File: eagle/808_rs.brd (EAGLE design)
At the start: 100 x 80 mm, 75 parts, among them IC1 TL072P, IC2 TL072P, Q1 2SK30, Q59 2N3904, Q60 2N3906, Q61 2N3904, Q62 2N3904, Q63 2N3904, SW8 808_LT_MSS42_SW_4PDT

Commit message: 95pct auto
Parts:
- C113: device TR808clone:C050-024X044 -> TR808clone:C075-032X103
- C114: device TR808clone:C035-025X75 -> TR808clone:C050-030X075
- C121: device TR808clone:C035-025X75 -> TR808clone:C050-025X075
- C4: device TR808clone:C025-025X050 -> TR808clone:C050-024X044
- D61, D63, D64: value 1N4148DO35-7 -> 1N4148DO35-10; device TR808clone:DO35-7 -> TR808clone:DO35-10
- R303, R309, R330: device TR808clone:0207/5V -> TR808clone:0207/2V
- R316: device TR808clone:0207/7 -> TR808clone:0207/5V
- R321: device TR808clone:0207/5V -> TR808clone:0207/7
- R326: device TR808clone:0207/7 -> TR808clone:0309/10
- moved C2 7.62 mm to (67.3, 15.2), turned to 90 degrees
- moved Q61 6.84 mm to (22.9, 15.2)
- moved C112 5.68 mm to (30.5, 19.1), turned to 90 degrees
- moved R238 5.68 mm to (76.2, 20.3), turned to 180 degrees
- moved R304 5.39 mm to (24.1, 21.6)
- moved R305 5.24 mm to (43.2, 20.3)
- moved C153 4.02 mm to (61.0, 15.2)
- moved IC2 4.02 mm to (61.0, 21.6)
- moved R330 4.02 mm to (61.0, 12.7)
- moved OUT_NORM 4.02 mm to (77.5, 14.0), turned to 90 degrees
- moved R331 4.02 mm to (50.8, 20.3)
- moved C113 3.81 mm to (47.0, 20.3)
- moved C121 3.81 mm to (34.3, 36.8)
- moved C4 2.84 mm to (53.3, 26.7), turned to 180 degrees
- moved R316 2.84 mm to (63.5, 53.3)
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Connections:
- net N$172: now also C121.1; no longer C121.P$1
- net N$173: now also C114.1; no longer C114.P$1
- net N$328: now also C121.2; no longer C121.P$2
- net N$357: now also C114.2; no longer C114.P$2
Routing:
- net -12V: track 28.9 -> 268.6 mm
- net GND: track 346.2 -> 255.4 mm
- net N$357: track 44.0 -> 110.3 mm
- net N$338: track 120.2 -> 64.0 mm
- net N$351: track 87.8 -> 65.8 mm
- net N$348: track 50.0 -> 34.2 mm
- net +12V: track 101.4 -> 89.6 mm
- net N$8: track 108.3 -> 117.2 mm
- net N$328: track 13.4 -> 8.74 mm
- net N$173: track 12.7 -> 8.15 mm
- net N$353: track 14.0 -> 10.4 mm
- net N$161: track 31.1 -> 34.0 mm
- net N$344: track 30.7 -> 27.8 mm
- net N$354: track 12.7 -> 10.2 mm
- net N$352: track 8.75 -> 6.35 mm
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
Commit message: 94pct auto
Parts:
- C118: device TR808clone:C035-025X75 -> TR808clone:C050-024X044
- C122: device TR808clone:C035-025X75 -> TR808clone:C050-030X075
- R318: device TR808clone:0207/2V -> TR808clone:0207/5V
- R320, R322: device TR808clone:0207/5V -> TR808clone:0207/7
- moved R316 6.48 mm to (57.1, 54.6), turned to 180 degrees
- moved R320 5.39 mm to (72.4, 49.5), turned to 270 degrees
- moved R299 5.08 mm to (16.5, 55.9), turned to 180 degrees
- moved R318 4.58 mm to (64.8, 54.6)
- moved C120 3.81 mm to (38.1, 25.4)
- moved ACCENT 3.81 mm to (17.8, 59.7)
- moved R301 2.84 mm to (48.3, 61.0)
- moved C125 2.84 mm to (81.3, 40.6)
- moved R317 2.84 mm to (69.8, 58.4)
- moved R238 2.84 mm to (78.7, 19.1)
- moved R297 2.54 mm to (7.62, 54.6), turned to 90 degrees
- moved C115 2.54 mm to (58.4, 58.4)
- moved C116 2.54 mm to (55.9, 58.4)
- moved Q62 2.54 mm to (40.6, 31.8)
- moved R310 2.54 mm to (43.2, 38.1)
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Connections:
- net N$165: now also C118.2; no longer C118.P$2
- net N$328: now also C122.1; no longer C122.P$1
- net N$329: now also C122.2; no longer C122.P$2
- net N$340: now also C118.1; no longer C118.P$1
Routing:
- net -12V: track 268.6 -> 0.00 mm
- net GND: track 255.4 -> 0.00 mm
- net N$8: track 117.2 -> 0.00 mm
- net N$357: track 110.3 -> 0.00 mm
- net +12V: track 89.6 -> 0.00 mm
- net N$6: track 66.3 -> 0.00 mm
- net N$351: track 65.8 -> 0.00 mm
- net N$338: track 64.0 -> 0.00 mm
- net N$355: track 44.8 -> 0.00 mm
- net TRIG: track 42.1 -> 0.00 mm
- net RS: track 35.3 -> 0.00 mm
- net N$348: track 34.2 -> 0.00 mm
- net N$161: track 34.0 -> 0.00 mm
- net N$165: track 28.6 -> 0.00 mm
- net N$344: track 27.8 -> 0.00 mm
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
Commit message: routed
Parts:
- C1: device TR808clone:C025-025X050 -> TR808clone:C050-024X044
- C112, C118: device TR808clone:C050-024X044 -> TR808clone:C050-025X075
- C113: device TR808clone:C075-032X103 -> TR808clone:C050-025X075
- C117, C119: device TR808clone:C035-025X75 -> TR808clone:C050-024X044
- C120: device TR808clone:E2,5-5 -> TR808clone:E2,5-6
- C125: device TR808clone:C035-025X75 -> TR808clone:C050-025X075
- R312, R314, R318: device TR808clone:0207/5V -> TR808clone:0207/7
- R331: device TR808clone:0207/7 -> TR808clone:0207/5V
- moved SW8 107.3 mm to (0.00, 14.0), turned to 270 degrees
- moved OUTPUT 103.5 mm to (0.00, 45.7), turned to 90 degrees
- moved VR16 92.7 mm to (3.81, 34.3), turned to 270 degrees
- moved R303 88.8 mm to (92.7, 19.1), turned to 270 degrees
- moved R297 88.4 mm to (92.7, 30.5), turned to 180 degrees
- moved U$1 86.1 mm to (90.2, 49.5), turned to 270 degrees
- moved ACCENT 83.9 mm to (82.5, 6.35), turned to 180 degrees
- moved R298 83.0 mm to (86.4, 12.7), turned to 180 degrees
- moved R299 81.4 mm to (83.8, 10.2), turned to 0 degrees
- moved TRIGGER 80.1 mm to (87.6, 31.5), turned to 180 degrees
- moved Q59 80.0 mm to (87.6, 19.1), turned to 270 degrees
- moved R306 77.3 mm to (89.2, 26.7), turned to 0 degrees
- moved Q60 71.7 mm to (81.3, 15.2), turned to 180 degrees
- moved C111 71.0 mm to (74.9, 6.35), turned to 270 degrees
- moved C114 70.8 mm to (83.6, 21.6), turned to 270 degrees
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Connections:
- net N$2: now also C125.1; no longer C125.P$1
- net N$338: now also C117.2, C119.1; no longer C117.P$2, C119.P$1
- net N$339: now also C119.2; no longer C119.P$2
- net N$340: now also C117.1; no longer C117.P$1
- net N$347: now also C125.2; no longer C125.P$2
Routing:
- net GND: track 0.00 -> 336.7 mm, vias 0 -> 2
- net +12V: track 0.00 -> 168.5 mm, vias 0 -> 6
- net -12V: track 0.00 -> 121.3 mm
- net N$8: track 0.00 -> 117.8 mm, vias 0 -> 2
- net N$351: track 0.00 -> 79.6 mm
- net N$6: track 0.00 -> 67.2 mm
- net N$355: track 0.00 -> 61.3 mm, vias 0 -> 2
- net N$338: track 0.00 -> 54.7 mm
- net N$357: track 0.00 -> 49.2 mm
- net TRIG: track 0.00 -> 46.0 mm
- net N$348: track 0.00 -> 37.5 mm
- net N$344: track 0.00 -> 31.4 mm
- net N$165: track 0.00 -> 27.3 mm
- net N$161: track 0.00 -> 21.1 mm
- net N$318: track 0.00 -> 18.1 mm
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
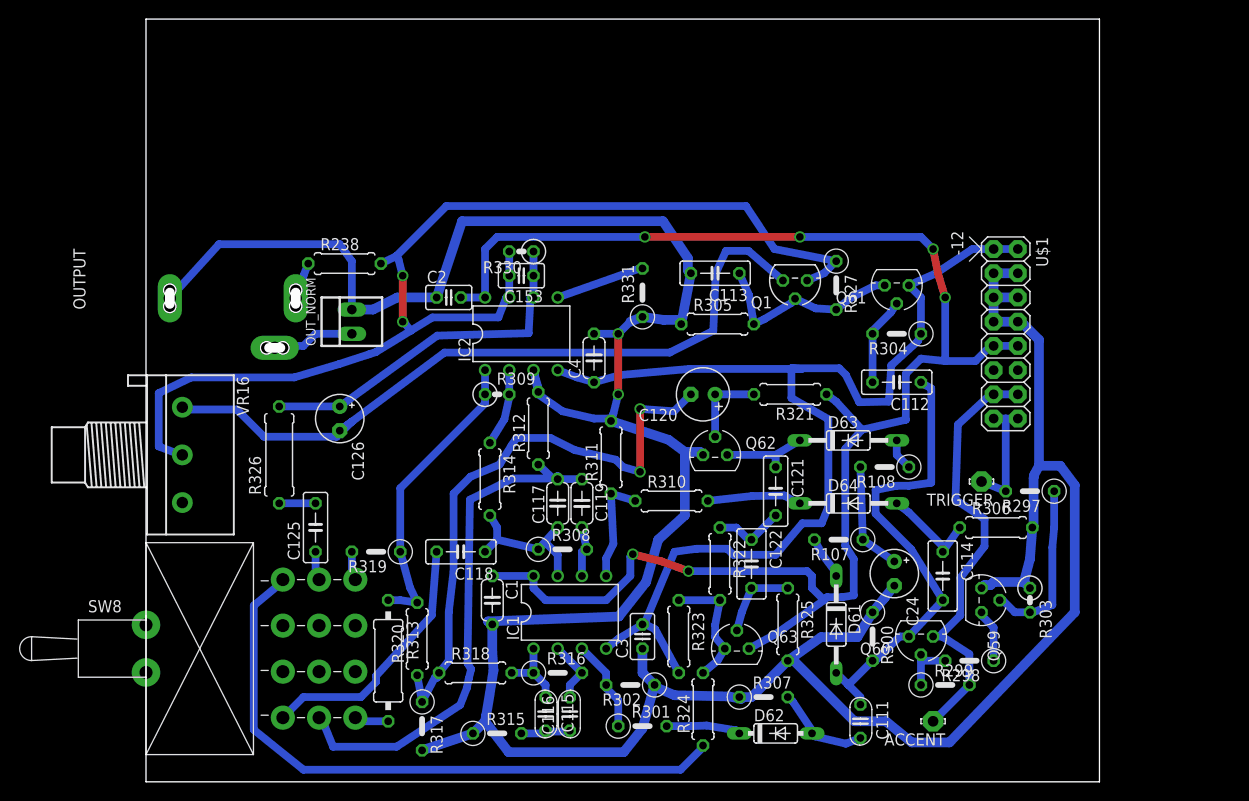
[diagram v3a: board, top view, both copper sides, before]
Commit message: almost rerouted
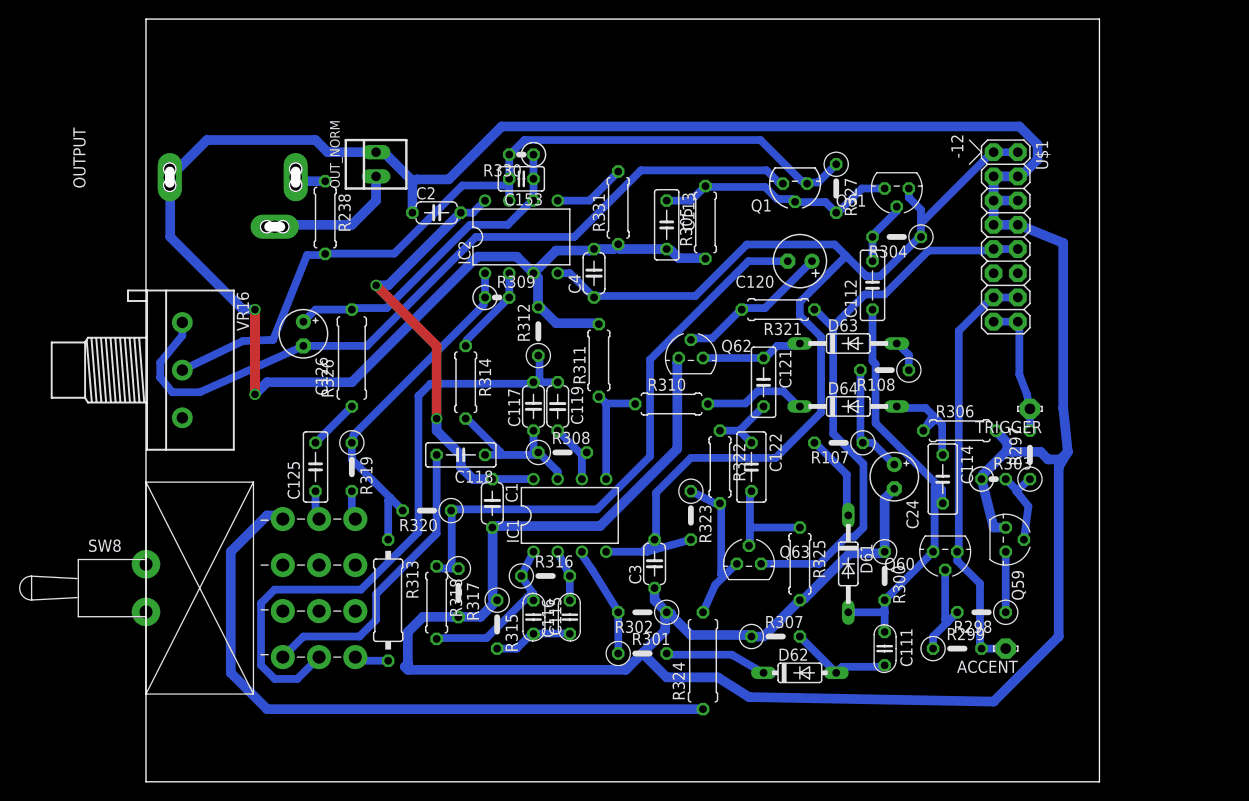
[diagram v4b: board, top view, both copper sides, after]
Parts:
- C2, C3: device TR808clone:C025-025X050 -> TR808clone:C050-024X044
- R312, R320, R323: device TR808clone:0207/7 -> TR808clone:0207/5V
- R324: device TR808clone:0207/7 -> TR808clone:0309/10
- R331: device TR808clone:0207/5V -> TR808clone:0207/7
- moved C120 17.3 mm to (68.6, 54.6)
- moved OUT_NORM 16.7 mm to (24.1, 64.8)
- moved R317 14.5 mm to (32.8, 19.8)
- moved R320 13.5 mm to (29.5, 28.4), turned to 180 degrees
- moved R303 13.3 mm to (88.9, 31.8), turned to 0 degrees
- moved R323 12.8 mm to (57.1, 27.9)
- moved OUTPUT 12.7 mm to (0.00, 58.4)
- moved R326 12.7 mm to (21.6, 44.5)
- moved C121 11.5 mm to (64.8, 41.9)
- moved R315 11.4 mm to (36.8, 16.5), turned to 270 degrees
- moved R306 10.9 mm to (85.3, 36.8)
- moved ACCENT 10.8 mm to (90.2, 14.0)
- moved R305 10.7 mm to (58.7, 58.7), turned to 90 degrees
- moved Q62 10.5 mm to (57.1, 44.5)
- moved C112 10.5 mm to (76.2, 52.1), turned to 90 degrees
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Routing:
- net GND: track 336.7 -> 450.6 mm
- net +12V: track 168.5 -> 106.2 mm, vias 6 -> 2
- net N$8: track 117.8 -> 86.6 mm, vias 2 -> 0
- net N$338: track 54.7 -> 66.1 mm
- net N$354: track 7.92 -> 18.0 mm
- net N$318: track 18.1 -> 9.20 mm
- net N$174: track 8.51 -> 16.1 mm
- net N$344: track 31.4 -> 37.3 mm
- net N$5: track 8.70 -> 14.3 mm
- net N$317: track 5.71 -> 10.4 mm
- net N$324: track 4.50 -> 9.10 mm
- net N$161: track 21.1 -> 25.6 mm
- net N$357: track 49.2 -> 44.9 mm
- net N$330: track 13.3 -> 17.5 mm
- net N$165: track 27.3 -> 31.3 mm
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
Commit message: rerouted
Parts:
- R320: device TR808clone:0207/5V -> TR808clone:0207/7
- moved C120 17.0 mm to (53.3, 47.0), turned to 270 degrees
- moved R107 4.31 mm to (75.7, 32.5)
- moved R314 4.10 mm to (37.6, 41.4)
- moved C24 3.84 mm to (79.0, 28.2)
- moved R323 2.54 mm to (57.1, 25.4)
- moved Q62 1.78 mm to (58.9, 44.5)
- moved C122 1.61 mm to (65.0, 33.5)
- moved R321 1.30 mm to (67.6, 49.8)
- moved R310 1.27 mm to (53.8, 39.6)
- moved R322 1.27 mm to (61.5, 33.0)
- moved R324 1.27 mm to (58.4, 14.0)
- moved R312 1.08 mm to (41.9, 46.5)
- moved R301 1.02 mm to (52.1, 14.5)
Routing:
- net +12V: track 106.2 -> 173.0 mm, vias 2 -> 4
- net N$355: track 60.6 -> 43.5 mm
- net -12V: track 119.0 -> 111.9 mm
- net GND: track 450.6 -> 444.4 mm
- net N$173: track 12.0 -> 7.14 mm
- net N$324: track 9.10 -> 4.79 mm
- net N$357: track 44.9 -> 48.1 mm
- net N$167: track 12.0 -> 15.0 mm
- net N$174: track 16.1 -> 13.4 mm
- net N$6: track 71.0 -> 68.5 mm
- net N$338: track 66.1 -> 63.9 mm
- net N$340: track 17.5 -> 15.4 mm
- net N$172: track 10.8 -> 9.03 mm
- net N$336: track 10.8 -> 12.3 mm
- net N$8: track 86.6 -> 88.0 mm
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
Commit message: tweaks
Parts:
- R305, R318: device TR808clone:0207/7 -> TR808clone:0207/5V
- R313: device TR808clone:0309/12 -> TR808clone:0207/7
- R316: device TR808clone:0207/5V -> TR808clone:0207/2V
- R324: device TR808clone:0309/10 -> TR808clone:0207/7
- moved R318 6.67 mm to (35.6, 23.1), turned to 0 degrees
- moved C2 4.23 mm to (32.8, 63.2), turned to 270 degrees
- moved R330 3.70 mm to (42.9, 64.8), turned to 90 degrees
- moved R305 3.18 mm to (57.1, 55.9), turned to 0 degrees
- moved R317 2.84 mm to (32.3, 17.0)
- moved C113 2.34 mm to (56.9, 58.9), turned to 180 degrees
- moved R321 2.03 mm to (69.6, 49.8)
- moved R313 1.55 mm to (25.1, 17.5)
- moved R325 1.02 mm to (67.6, 22.9)
- moved Q59 0.92 mm to (89.4, 25.9)
- moved R324 0.80 mm to (58.7, 13.2)
- moved R316 0.57 mm to (42.2, 21.1)
- moved C114 0.51 mm to (83.1, 31.8)
- moved R108 0.25 mm to (77.2, 43.2)
- moved D61 0.25 mm to (73.4, 22.9)
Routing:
- net GND: track 444.4 -> 427.5 mm
- net N$354: track 18.0 -> 8.42 mm
- net N$338: track 63.9 -> 55.9 mm
- net N$344: track 36.7 -> 40.8 mm
- net N$174: track 13.4 -> 17.5 mm
- net N$8: track 88.0 -> 85.1 mm
- net +12V: track 173.0 -> 170.4 mm
- net N$161: track 26.4 -> 23.9 mm
- net N$330: track 18.5 -> 19.9 mm
- net N$329: track 12.0 -> 10.9 mm
- net N$165: track 31.9 -> 32.9 mm
- net N$318: track 9.02 -> 8.32 mm
- net -12V: track 111.9 -> 111.3 mm
- net N$319: track 6.35 -> 6.90 mm
